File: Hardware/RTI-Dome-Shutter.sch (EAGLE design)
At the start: 42 parts, among them IC1 24AA128ST, IC5 74LVC245, IC6 74ABT245, J1 POWERPOLE_POWER45A

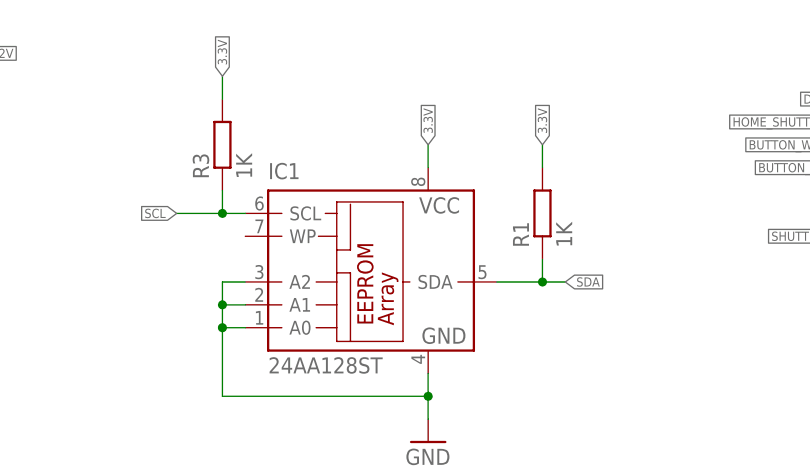
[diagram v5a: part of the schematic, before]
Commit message: Fix a few component values.
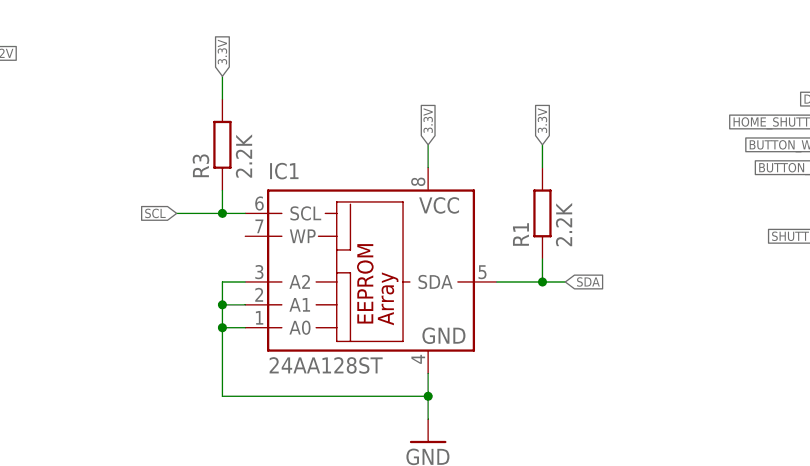
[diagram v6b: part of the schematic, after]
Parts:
- R1, R3: value 1K -> 2.2K
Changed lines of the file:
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@@
 <part name="IC1" library="microchip" deviceset="24*" device="ST" technology="AA128"/>
 <part name="GND8" library="supply1" deviceset="GND" device=""/>
-<part name="R1" library="rti" deviceset="R-EU" device="'0805'" value="1K"/>
-<part name="R3" library="rti" deviceset="R-EU" device="'0805'" value="1K"/>
+<part name="R1" library="rti" deviceset="R-EU" device="'0805'" value="2.2K"/>
+<part name="R3" library="rti" deviceset="R-EU" device="'0805'" value="2.2K"/>
 <part name="C5" library="rti" deviceset="C-EU" device="'0805'" value="100nF"/>
 <part name="GND12" library="supply1" deviceset="GND" device=""/>
